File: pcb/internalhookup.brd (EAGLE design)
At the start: 26.6 x 16.2 mm, 8 parts, among them CN1 LASER, J2 SERVO, J5 CONTROL, Q1 600mA/40V, U1 AMS1117-3.3

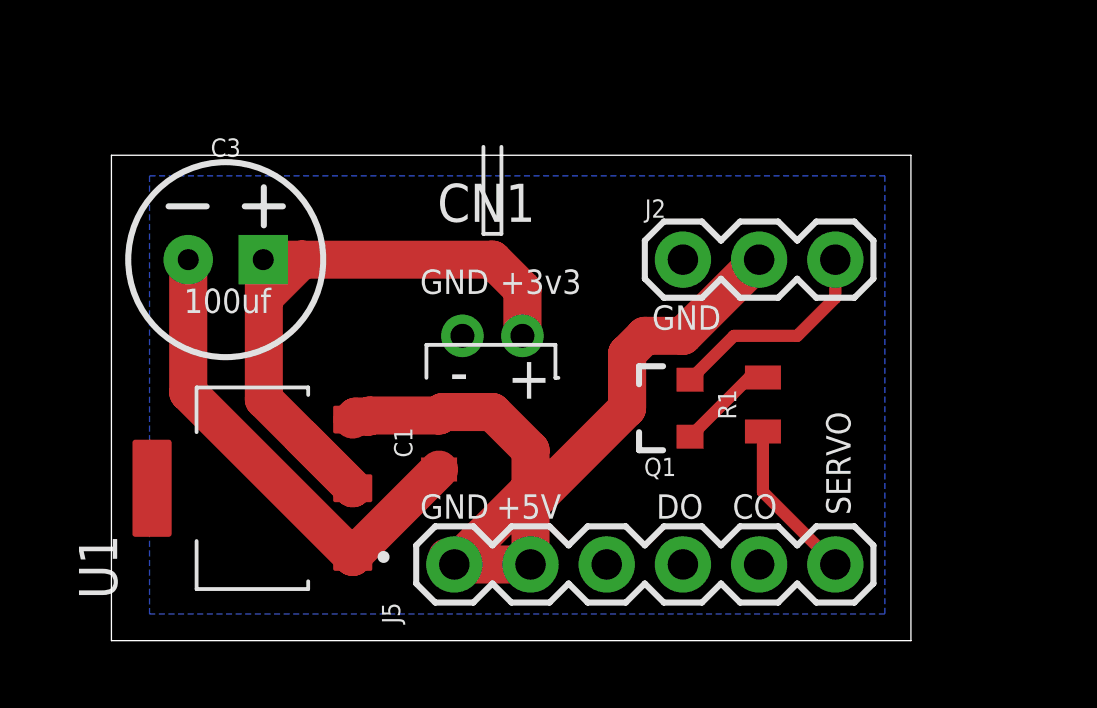
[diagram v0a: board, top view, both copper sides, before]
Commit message: Version 47:
* Only wake motor from sleep IFF we are going to move the motor
* Clean up some extra logging
* Add LED controls for the globe lighting
* This includes the first PCB sent out for production at OSHPark
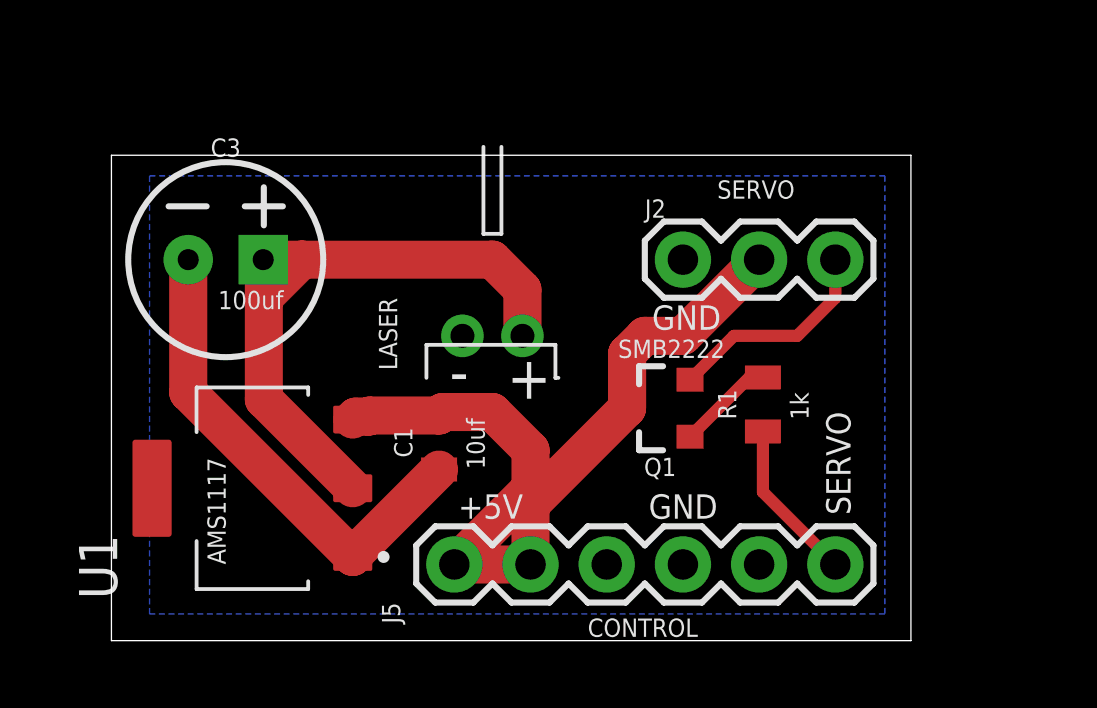
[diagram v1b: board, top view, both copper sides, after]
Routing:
- net +3V3: track 23.6 -> 21.2 mm
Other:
- board text added: "10uf"
- board text added: "1k"
- board text added: "AMS1117"
- board text added: "CONTROL"
- board text added: "ISS Hookup (C) Peter Buelow Jan 2021 Version 1.0"
- board text added: "LASER"
- board text added: "SMB2222"
- board text removed: "+3v3"
- board text removed: "CO"
- board text removed: "DO"
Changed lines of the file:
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@@
 <layer number="118" name="Rect_Pads" color="7" fill="1" visible="yes" active="yes"/>
 <layer number="121" name="_tsilk" color="7" fill="1" visible="yes" active="yes"/>
-<layer number="122" name="_bsilk" color="7" fill="1" visible="yes" active="yes"/>
+<layer number="122" name="_bsilk" color="7" fill="1" visible="no" active="yes"/>
 <layer number="123" name="tTestmark" color="7" fill="1" visible="yes" active="yes"/>
 <layer number="124" name="bTestmark" color="7" fill="1" visible="yes" active="yes"/>
@@
 <wire x1="26.65" y1="16.18" x2="0" y2="16.18" width="0" layer="20"/>
 <wire x1="0" y1="16.18" x2="0" y2="0" width="0" layer="20"/>
-<text x="12.954" y="11.557" size="0.8128" layer="121">+3v3</text>
-<text x="12.827" y="4.064" size="0.8128" layer="121">+5V</text>
-<text x="10.287" y="11.557" size="0.8128" layer="121">GND</text>
+<text x="11.557" y="4.064" size="0.8128" layer="121">+5V</text>
 <text x="20.32" y="11.176" size="0.8128" layer="121" rot="R180">GND</text>
-<text x="10.287" y="4.064" size="0.8128" layer="121">GND</text>
-<text x="18.161" y="4.064" size="0.8128" layer="121">DO</text>
-<text x="20.701" y="4.064" size="0.8128" layer="121">CO</text>
+<text x="17.907" y="4.064" size="0.8128" layer="121">GND</text>
 <text x="24.638" y="4.191" size="0.8128" layer="121" rot="R90">SERVO</text>
-<text x="2.413" y="10.922" size="0.8128" layer="112">100uf</text>
+<text x="25.4" y="5.08" size="1.016" layer="122" rot="MR0">ISS Hookup
+(C) Peter Buelow
+Jan 2021
+Version 1.0</text>
+<text x="12.446" y="5.715" size="0.6096" layer="121" rot="R90">10uf</text>
+<text x="20.193" y="14.732" size="0.6096" layer="121">SERVO</text>
+<text x="15.875" y="0.127" size="0.6096" layer="121">CONTROL</text>
+<text x="23.241" y="7.366" size="0.6096" layer="121" rot="R90">1k</text>
+<text x="3.81" y="2.54" size="0.6096" layer="121" rot="R90">AMS1117</text>
+<text x="9.525" y="9.017" size="0.6096" layer="121" rot="R90">LASER</text>
+<text x="20.447" y="10.033" size="0.6096" layer="121" rot="R180">SMB2222</text>
+<text x="3.556" y="11.049" size="0.6096" layer="121">100uf</text>
 </plain>
 <attributes>
@@
 <element name="J2" library="SparkFun-Connectors" library_urn="urn:adsk.eagle:library:513" package="1X03" package3d_urn="urn:adsk.eagle:package:38063/1" value="SERVO" x="19.05" y="12.7" smashed="yes">
 <attribute name="NAME" x="17.78" y="14.097" size="0.6096" layer="25" font="vector" ratio="20"/>
-<attribute name="VALUE" x="20.447" y="14.224" size="0.6096" layer="27" font="vector" ratio="20"/>
 </element>
 <element name="R1" library="SparkFun-Resistors" library_urn="urn:adsk.eagle:library:532" package="0805" package3d_urn="urn:adsk.eagle:package:39651/1" value="1k" x="21.717" y="7.874" smashed="yes" rot="R90">
 <attribute name="NAME" x="20.828" y="7.874" size="0.6096" layer="25" font="vector" ratio="20" rot="R90" align="bottom-center"/>
 <attribute name="PROD_ID" value="RES-11622" x="21.717" y="7.874" size="1.778" layer="27" rot="R90" display="off"/>
-<attribute name="VALUE" x="22.606" y="7.874" size="0.6096" layer="27" font="vector" ratio="20" rot="R90" align="top-center"/>
 </element>
 <element name="Q1" library="SparkFun-DiscreteSemi" library_urn="urn:adsk.eagle:library:514" package="SOT23-3" package3d_urn="urn:adsk.eagle:package:38446/1" value="600mA/40V" x="18.288" y="7.747" smashed="yes" rot="R90">
@@
 <attribute name="NAME" x="9.017" y="1.27" size="0.6096" layer="25" font="vector" ratio="20" rot="R270"/>
 <attribute name="PROD_ID" value="CONN-08437" x="24.13" y="2.54" size="0.8128" layer="27" rot="R180" display="off"/>
-<attribute name="VALUE" x="25.4" y="4.572" size="0.6096" layer="27" font="vector" ratio="20" rot="R180"/>
-</element>
-<element name="CN1" library="adafruit" library_urn="urn:adsk.eagle:library:420" package="JST-PH-2-THM-RA" package3d_urn="urn:adsk.eagle:package:6240694/1" value=" LASER" x="12.7" y="10.16" smashed="yes">
-<attribute name="NAME" x="14.13" y="15.23" size="1.27" layer="25" font="vector" rot="R180"/>
-</element>
+</element>
+<element name="CN1" library="adafruit" library_urn="urn:adsk.eagle:library:420" package="JST-PH-2-THM-RA" package3d_urn="urn:adsk.eagle:package:6240694/1" value=" LASER" x="12.7" y="10.16" smashed="yes"/>
 <element name="C1" library="SparkFun-Capacitors" library_urn="urn:adsk.eagle:library:510" package="0805" package3d_urn="urn:adsk.eagle:package:37429/1" value="10uf" x="10.922" y="6.604" smashed="yes" rot="R90">
 <attribute name="NAME" x="10.033" y="6.604" size="0.6096" layer="25" font="vector" ratio="20" rot="R90" align="bottom-center"/>
 <attribute name="PROD_ID" value="CAP-08064" x="10.922" y="6.604" size="0.4064" layer="27" rot="R90" display="off"/>
-<attribute name="VALUE" x="11.811" y="6.604" size="0.6096" layer="27" font="vector" ratio="20" rot="R90" align="top-center"/>
 </element>
 <element name="U1" library="AMS1117-3.3" package="SOT229P700X180-4N" value="AMS1117-3.3" x="4.699" y="5.08" smashed="yes" rot="R90">
@@
 <contactref element="J5" pad="3"/>
 <contactref element="J5" pad="2"/>
-<wire x1="19.05" y1="2.54" x2="21.59" y2="2.54" width="0" layer="19" extent="1-1"/>
-<wire x1="16.51" y1="2.54" x2="19.05" y2="2.54" width="0" layer="19" extent="1-1"/>
 </signal>
 <signal name="+5V">
@@
 <contactref element="C1" pad="2"/>
 <contactref element="J5" pad="6"/>
-<wire x1="11.19" y1="2.78" x2="11.43" y2="2.54" width="1.27" layer="1"/>
 <wire x1="11.43" y1="2.54" x2="13.97" y2="2.54" width="1.27" layer="1"/>
 <contactref element="U1" pad="3"/>
@@
 <contactref element="U1" pad="2"/>
 <wire x1="5.08" y1="8.044" x2="8.044" y2="5.08" width="1.27" layer="1"/>
-<wire x1="6.35" y1="6.774" x2="8.044" y2="5.08" width="1.27" layer="1"/>
 <wire x1="5.06" y1="12.7" x2="5.08" y2="12.68" width="1.27" layer="1"/>
 <wire x1="5.08" y1="12.68" x2="5.08" y2="11.43" width="1.27" layer="1"/>
@@
 </drawing>
 <compatibility>
+<note version="6.3" minversion="6.2.2" severity="warning">
+Since Version 6.2.2 text objects can contain more than one line,
+which will not be processed correctly with this version.
+</note>
 <note version="8.2" severity="warning">
 Since Version 8.2, EAGLE supports online libraries. The ids

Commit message: Updating to the latest PCB to fix breaking issues
* Fixed capacitor sets for both boards to be larger and polarized on the
LDO's
* Fixed left track for motor board as it was 1 pin too short
* Switched from Declination to Azimuth
* Moved Azimuth signaling to the internal board to allow for movement
* Removed resistors on 5V LED signal buffer
* Switch LED pinout to match the Lumenati ordering
* Internal board got a polarized capacitor
* Internal board layout moved around to better match reality
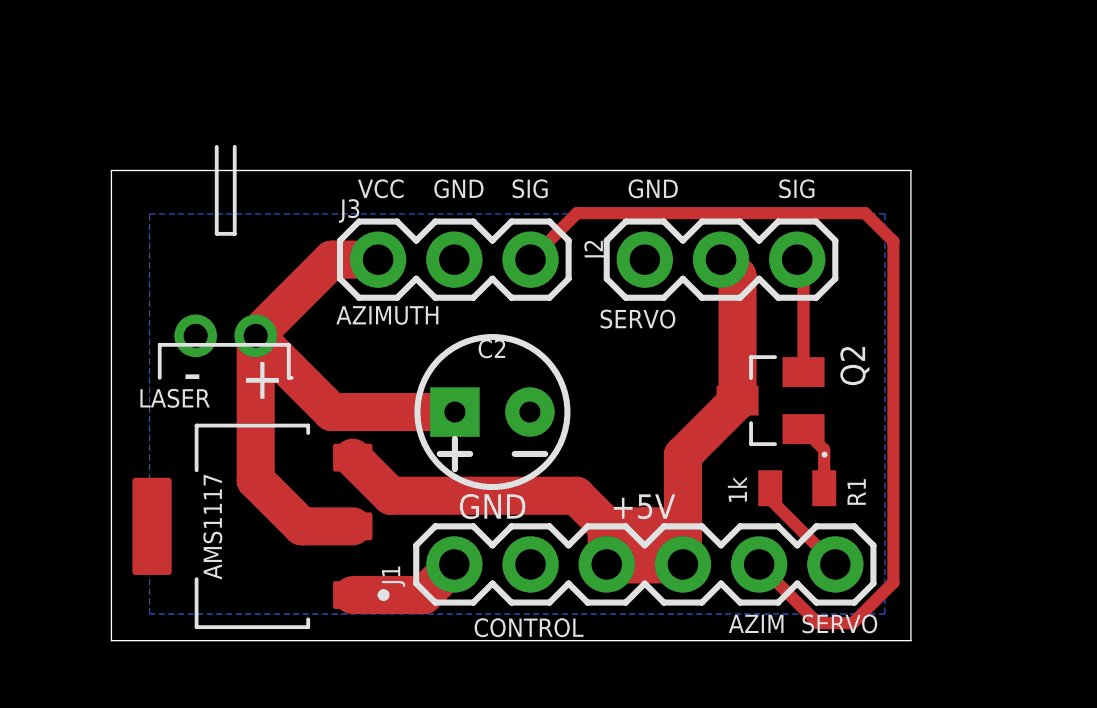
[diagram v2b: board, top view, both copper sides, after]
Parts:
- removed C1: 10uf, SparkFun-Capacitors:0805
- removed C3: 100uF, SparkFun-Capacitors:CPOL-RADIAL-2.5MM-6.5MM
- removed Q1: 600mA/40V, SparkFun-DiscreteSemi:SOT23-3
- added C2: 10uF, SparkFun-Capacitors:CPOL-RADIAL-2.5MM-5MM
- added J3: AZ_SENSOR, SparkFun-Connectors:1X03
- added Q2: SMMBT2222ALT, MMBT3904:SOT95P240X120-3N
- moved CN1 8.89 mm to (3.81, 10.2)
- moved R1 3.02 mm to (22.9, 5.08), turned to 0 degrees
- moved U1 1.27 mm to (4.70, 3.81)
- moved J2 1.27 mm to (17.8, 12.7)
- renumbered J5 to J1
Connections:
- new net AZIMUTH: J1.2, J3.3
- net +3V3: now also C2.1, J3.1; no longer C3.1
- net +5V: now also J1.3, J1.4, Q2.3; no longer C1.2, J1.5, J1.6, Q1.3
- net GND: now also C2.2, J1.5, J1.6, J3.2; no longer C1.1, C3.2, J1.2, J1.3, J1.4
- net N$1: now also Q2.1; no longer Q1.1
- net N$2: now also Q2.2; no longer Q1.2
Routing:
- net AZIMUTH: track 0.00 -> 30.3 mm
- net GND: track 16.3 -> 3.81 mm
- net N$2: track 7.24 -> 3.84 mm
- net +5V: track 28.6 -> 31.2 mm
- net SERVO: track 5.43 -> 3.44 mm
- net N$1: track 3.25 -> 2.26 mm
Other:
- board size 26.6 x 16.2 mm -> 26.6 x 15.7 mm
- board text added: "AZIM"
- board text added: "AZIMUTH"
- board text added: "ISS Control (C) Peter Buelow February 2021 Version 1.1"
- board text added: "SIG"
- board text added: "VCC"
- board text removed: "100uf"
- board text removed: "10uf"
- board text removed: "ISS Hookup (C) Peter Buelow Jan 2021 Version 1.0"
- board text removed: "SMB2222"

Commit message: Adding laser control
* Hookup an NPN to be able to turn the laser on/off via A0
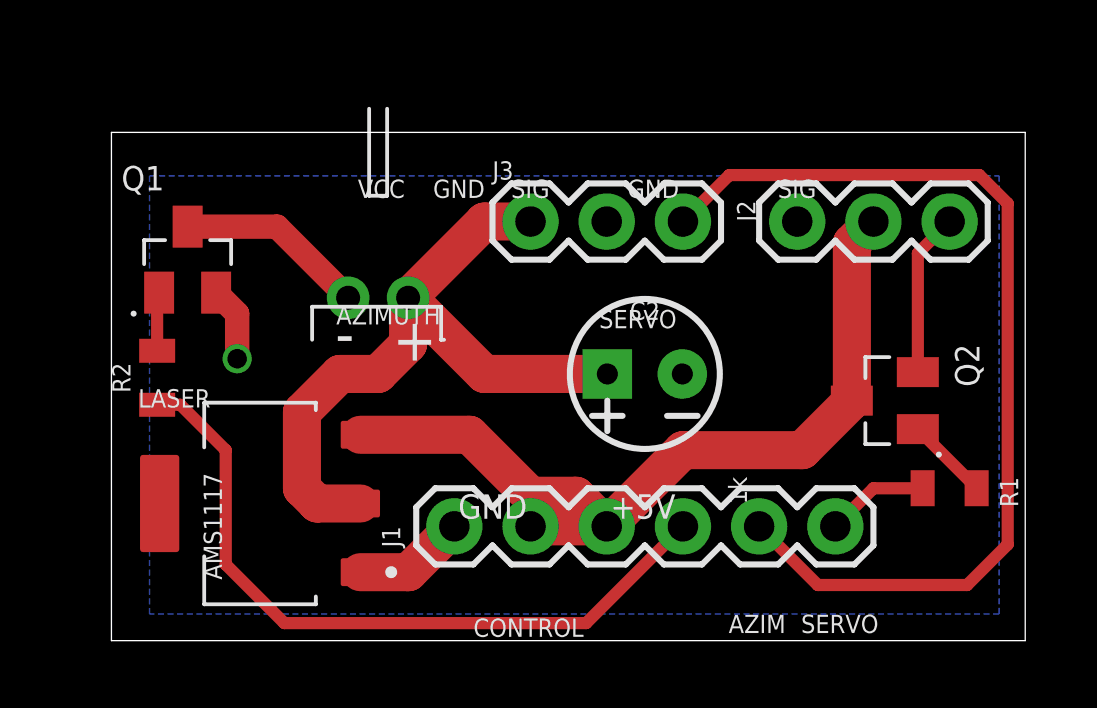
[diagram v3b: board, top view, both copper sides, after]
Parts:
- added Q1: SMMBT2222ALT, MMBT3904:SOT95P240X120-3N
- added R2: 1k, SparkFun-Resistors:0805
- moved C2 5.24 mm to (17.8, 8.89)
- moved CN1 5.24 mm to (8.89, 11.4)
- moved J3 5.24 mm to (14.0, 14.0)
- moved J2 5.24 mm to (22.9, 14.0)
- moved R1 5.08 mm to (27.9, 5.08)
- moved Q2 3.81 mm to (25.8, 8.00)
- moved J1 1.27 mm to (24.1, 3.81)
- moved U1 0.80 mm to (4.95, 4.57)
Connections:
- new net LASER: J1.3, R2.1
- new net LSR_GND: CN1.2, Q1.3
- new net N$3: Q1.1, R2.2
- net +5V: now also J1.5; no longer J1.3
- net GND: now also Q1.2; no longer CN1.2, J1.5
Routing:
- net LASER: track 0.00 -> 24.1 mm
- net LSR_GND: track 0.00 -> 6.33 mm
- net +5V: track 31.2 -> 28.2 mm
- net AZIMUTH: track 30.3 -> 32.9 mm
- net GND: track 3.81 -> 6.26 mm, vias 0 -> 1
- net +3V3: track 21.5 -> 23.5 mm
- net N$3: track 0.00 -> 1.96 mm
- net N$2: track 3.84 -> 5.46 mm
- net N$1: track 2.26 -> 2.78 mm
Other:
- board size 26.6 x 15.7 mm -> 30.5 x 16.9 mm
- board text added: "ISS Control (C) Peter Buelow February 2021 Version 1.2"
- board text removed: "ISS Control (C) Peter Buelow February 2021 Version 1.1"

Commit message: Lots of changes
* Dropped LED's and LASER control
* Renamed DECLINATION to AZIMUTH
* Moved AZIMUTH control hookup into the globe (it needs to spin freely)

I couldn't make the LED's fit and shine without casting shadows inside
the globe. Plus, there wasn't much room, and it required more wires to
make work. No a critical problem, but the challenges outweighed the
benefits. I'm going to water color paint the globe now.

I also removed the LASER control, the manufacturer said don't duty cycle
it, the built in controls take care of it. This isn't supposed to be on
constantly anyway.
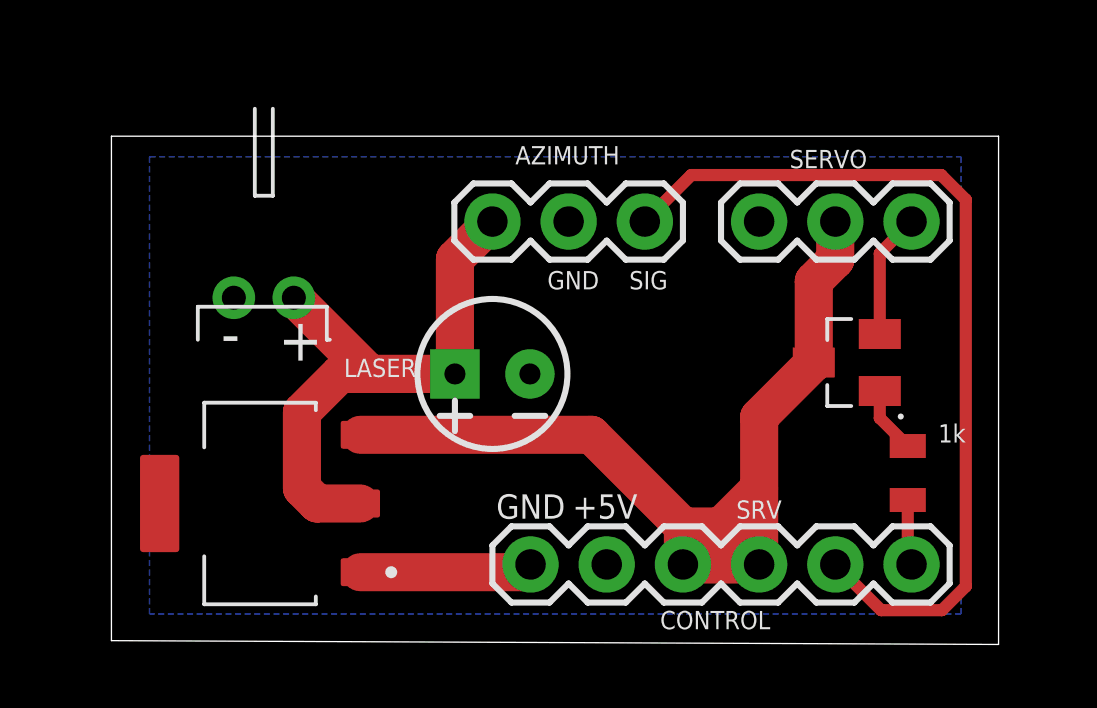
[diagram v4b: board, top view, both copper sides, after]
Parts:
- removed J3: AZ_SENSOR, SparkFun-Connectors:1X03
- removed Q1: SMMBT2222ALT, MMBT3904:SOT95P240X120-3N
- removed R2: 1k, SparkFun-Resistors:0805
- added J4: AZIMUTH, SparkFun-Connectors:1X03
- moved C2 5.08 mm to (12.7, 8.89)
- moved CN1 3.81 mm to (5.08, 11.4)
- moved J1 2.84 mm to (26.7, 2.54)
- moved Q2 1.80 mm to (24.5, 9.27)
- moved R1 1.49 mm to (26.5, 5.59), turned to 90 degrees
- moved J2 1.27 mm to (21.6, 14.0)
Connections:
- removed net LASER: J1.3, R2.1
- removed net LSR_GND: CN1.2, Q1.3
- removed net N$3: Q1.1, R2.2
- net +3V3: now also J4.1; no longer J3.1
- net +5V: now also J1.3; no longer J1.5
- net AZIMUTH: now also J4.3; no longer J3.3
- net GND: now also CN1.2, J1.5, J4.2; no longer J3.2, Q1.2
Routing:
- net LASER: track 24.1 -> 0.00 mm
- net LSR_GND: track 6.33 -> 0.00 mm
- net +5V: track 28.2 -> 32.6 mm
- net AZIMUTH: track 32.9 -> 29.9 mm
- net N$3: track 1.96 -> 0.00 mm
- net N$2: track 5.46 -> 4.19 mm
- net SERVO: track 3.44 -> 2.20 mm
- net +3V3: track 23.5 -> 22.3 mm
- net N$1: track 2.78 -> 2.22 mm
- net GND: track 6.26 -> 5.78 mm, vias 1 -> 0
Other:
- board size 30.5 x 16.9 mm -> 29.6 x 16.9 mm
- board text added: "ISS Control (C) Peter Buelow February 2021 Version 1.4"
- board text added: "SRV"
- board text removed: "AMS1117"
- board text removed: "AZIM"
- board text removed: "ISS Control (C) Peter Buelow February 2021 Version 1.2"
- board text removed: "VCC"
